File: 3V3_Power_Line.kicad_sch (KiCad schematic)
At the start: 11 parts, among them U3 LMR51625DDC

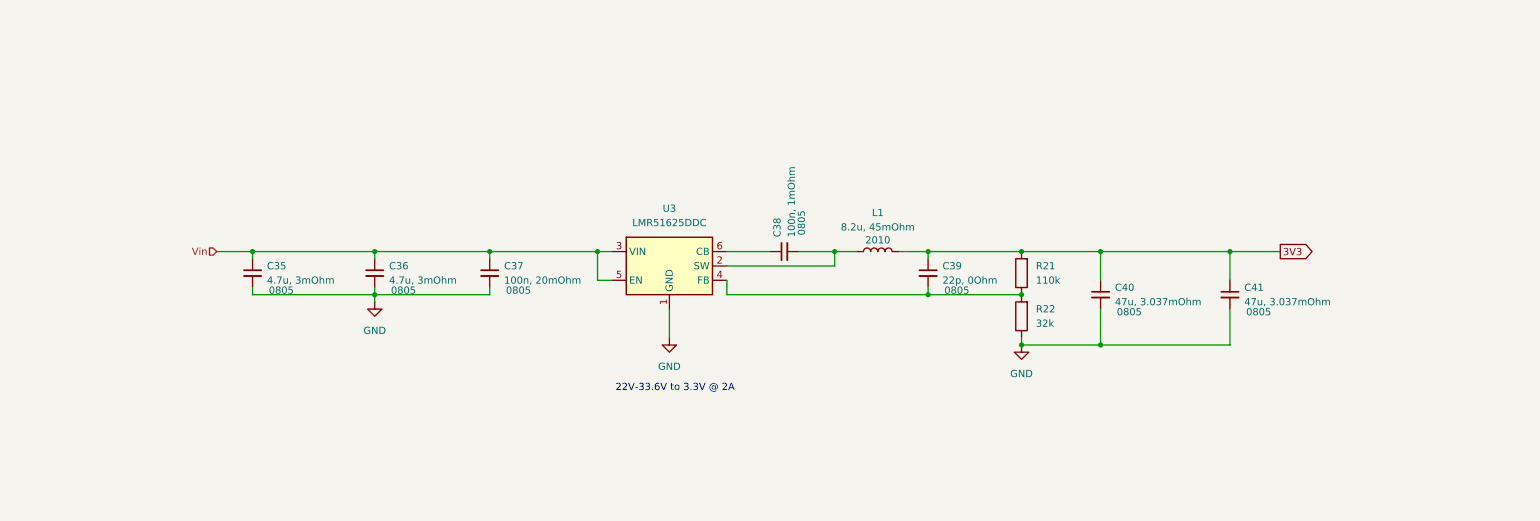
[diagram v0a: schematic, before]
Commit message: added more power lines
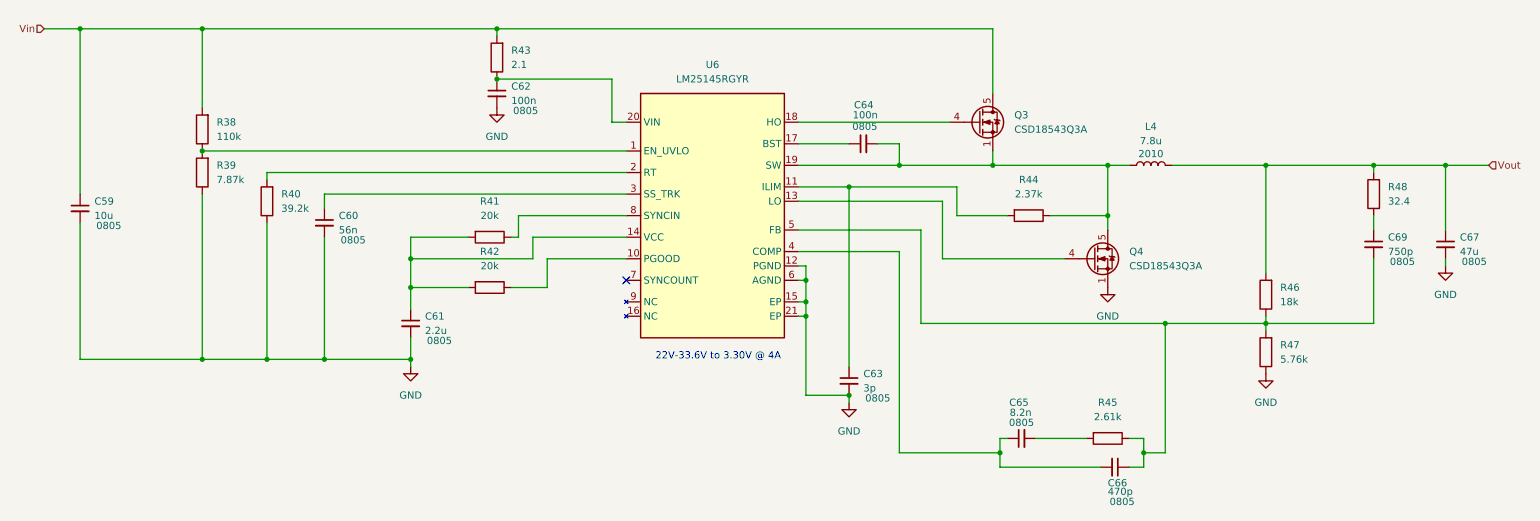
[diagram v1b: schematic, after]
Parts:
- removed C35, C36: 4.7u, 3mOhm, Capacitor_SMD:C_0805_2012Metric_Pad1.18x1.45mm_HandSolder, symbol Device:C_Small
- removed C37: 100n, 20mOhm, Capacitor_SMD:C_0805_2012Metric_Pad1.18x1.45mm_HandSolder, symbol Device:C_Small
- removed C38: 100n, 1mOhm, Capacitor_SMD:C_0805_2012Metric_Pad1.18x1.45mm_HandSolder, symbol Device:C_Small
- removed C39: 22p, 0Ohm, Capacitor_SMD:C_0805_2012Metric_Pad1.18x1.45mm_HandSolder, symbol Device:C_Small
- removed C40, C41: 47u, 3.037mOhm, Capacitor_SMD:C_0805_2012Metric_Pad1.18x1.45mm_HandSolder, symbol Device:C_Small
- removed L1: 8.2u, 45mOhm, Inductor_SMD_Wurth:L_Wurth_WE-LQSH-2010, symbol Device:L
- removed R21, R22: 150K_0603, PCM_4ms_Resistor:R_0805_2012Metric, symbol PCM_4ms_Resistor:150K_0603
- removed U3: LMR51625DDC, Package_TO_SOT_SMD:SOT-23-6, symbol Regulator_Switching:LMR51625DDC
- added C59: 10u, Capacitor_SMD:C_0805_2012Metric_Pad1.18x1.45mm_HandSolder, symbol Device:C_Small
- added C60: 56n, Capacitor_SMD:C_0805_2012Metric_Pad1.18x1.45mm_HandSolder, symbol Device:C_Small
- added C61: 2.2u, Capacitor_SMD:C_0805_2012Metric_Pad1.18x1.45mm_HandSolder, symbol Device:C_Small
- added C62, C64: 100n, Capacitor_SMD:C_0805_2012Metric_Pad1.18x1.45mm_HandSolder, symbol Device:C_Small
- added C63: 3p, Capacitor_SMD:C_0805_2012Metric_Pad1.18x1.45mm_HandSolder, symbol Device:C_Small
- added C65: 8.2n, Capacitor_SMD:C_0805_2012Metric_Pad1.18x1.45mm_HandSolder, symbol Device:C_Small
- added C66: 470p, Capacitor_SMD:C_0805_2012Metric_Pad1.18x1.45mm_HandSolder, symbol Device:C_Small
- added C67: 47u, Capacitor_SMD:C_0805_2012Metric_Pad1.18x1.45mm_HandSolder, symbol Device:C_Small
- added C69: 750p, Capacitor_SMD:C_0805_2012Metric_Pad1.18x1.45mm_HandSolder, symbol Device:C_Small
- added L4: 7.8u, Inductor_SMD_Wurth:L_Wurth_WE-LQSH-2010, symbol Device:L
- added Q3, Q4: CSD18543Q3A, Package_SON:VSON-8_3.3x3.3mm_P0.65mm_NexFET, symbol Transistor_FET:CSD18543Q3A
- added R38, R39, R40, R41, R42, R43, R44, R45, R46, R47, R48: 150K_0603, PCM_4ms_Resistor:R_0805_2012Metric, symbol PCM_4ms_Resistor:150K_0603
- added U6: LM25145RGYR, Project_Star_Regulator_Switching:RGY0020B, symbol Project_Star_Regulator_Switching:LM25145
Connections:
- net GND: now also C59.2, C60.2, C61.2, C62.2, C63.2, C67.2, Q4.1 (S), Q4.2 (S), Q4.3 (S), R39.1, R40.1, R47.1, U6.12 (PGND), U6.15 (EP), U6.21 (EP), U6.6 (AGND)
- net Vin: now also C59.1, Q3.5 (D), R38.2, R43.2
- new net: C66.1, C69.2, R45.1, R46.1, R47.2, U6.5 (FB)
- new net: C64.2, L4.1, Q3.1 (S), Q3.2 (S), Q3.3 (S), Q4.5 (D), R44.1, U6.19 (SW)
- new net: C63.1, R44.2, U6.11 (ILIM)
- new net: C61.1, R41.2, R42.2, U6.14 (VCC)
- new net: R38.1, R39.2, U6.1 (EN_UVLO)
- new net: C65.2, R45.2
- new net: C62.1, R43.1, U6.20 (VIN)
- new net: C60.1, U6.3 (SS_TRK)
- new net: C65.1, C66.2, U6.4 (COMP)
- new net: C64.1, U6.17 (BST)
- new net: R42.1, U6.10 (PGOOD)
- new net: Q4.4 (G), U6.13 (LO)
- new net: C69.1, R48.1
- new net: R40.2, U6.2 (RT)
- new net: Q3.4 (G), U6.18 (HO)
- new net: R41.1, U6.8 (SYNCIN)
- new net Vout: C67.1, L4.2, R46.2, R48.2
- no-connect marks 0 -> 1
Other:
- note added: "22V-33.6V to 3.30V @ 4A"
- note removed: "22V-33.6V to 3.3V @ 2A"

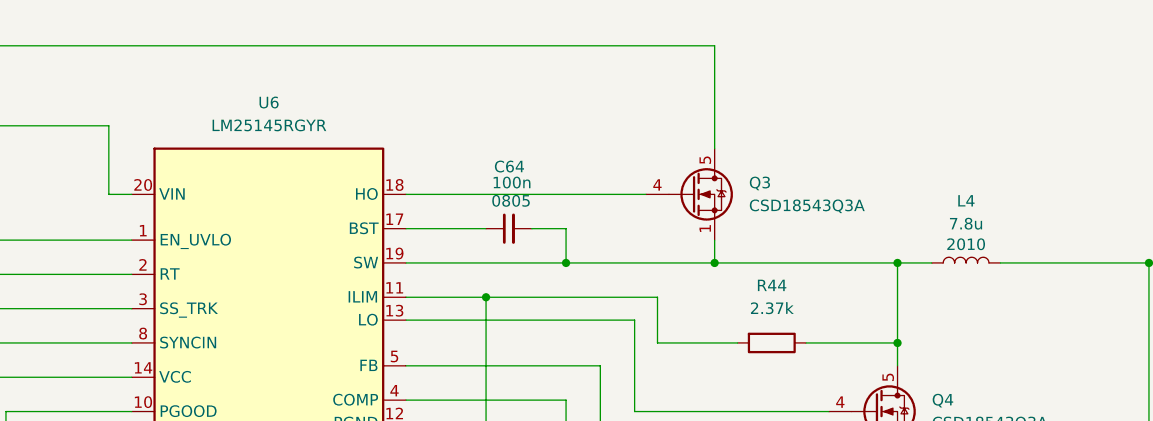
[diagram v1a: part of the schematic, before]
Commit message: 20V line PCB v1
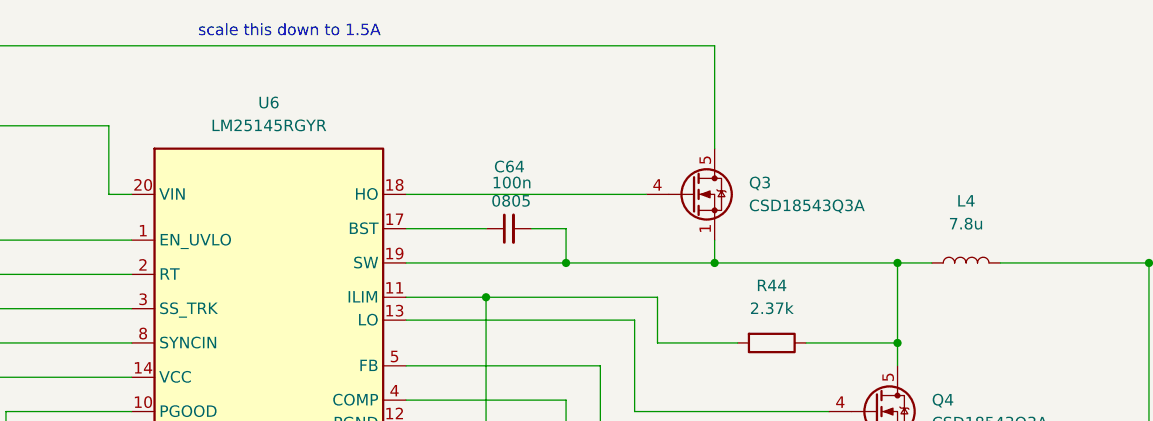
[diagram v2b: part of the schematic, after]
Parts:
- L4: footprint Inductor_SMD_Wurth:L_Wurth_WE-LQSH-2010 -> Inductor_THT:L_Radial_D10.0mm_P5.00mm_Fastron_07M
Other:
- note added: "scale this down to 1.5A"
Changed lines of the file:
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@@
 	(generator_version "9.0")
 	(paper "A4")
+	(text "scale this down to 1.5A"
+		(exclude_from_sim no)
+		(at 139.446 40.386 0)
+		(effects
+			(font
+				(size 1.27 1.27)
+			)
+		)
+	)
 	(text "22V-33.6V to 3.30V @ 4A"
 		(exclude_from_sim no)
@@
 			)
 		)
-		(property "Footprint" "Inductor_SMD_Wurth:L_Wurth_WE-LQSH-2010"
+		(property "Footprint" "Inductor_THT:L_Radial_D10.0mm_P5.00mm_Fastron_07M"
 			(at 214.63 66.04 0)
 			(effects
@@
 			)
 		)
-		(property "Description" "2010"
+		(property "Description" "6mm x 6mm"
 			(at 214.63 64.008 90)
 			(effects
@@
 					(size 1.27 1.27)
 				)
-			)
-		)
+				(hide yes)
+			)
+		)
